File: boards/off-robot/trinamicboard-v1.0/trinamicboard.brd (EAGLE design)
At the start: 133.7 x 89.7 mm, 57 parts, among them J4 DF22-2, J5 4-PIN_2MM-H, J6 MKS-1658, U1 ADC124S101, U2 SN74LVC3G17, U3 SN74LVC3G17, U4 VND5E006ASPTR-E, U5 MPM3620GQV-P, U6 MPM3620GQV-P

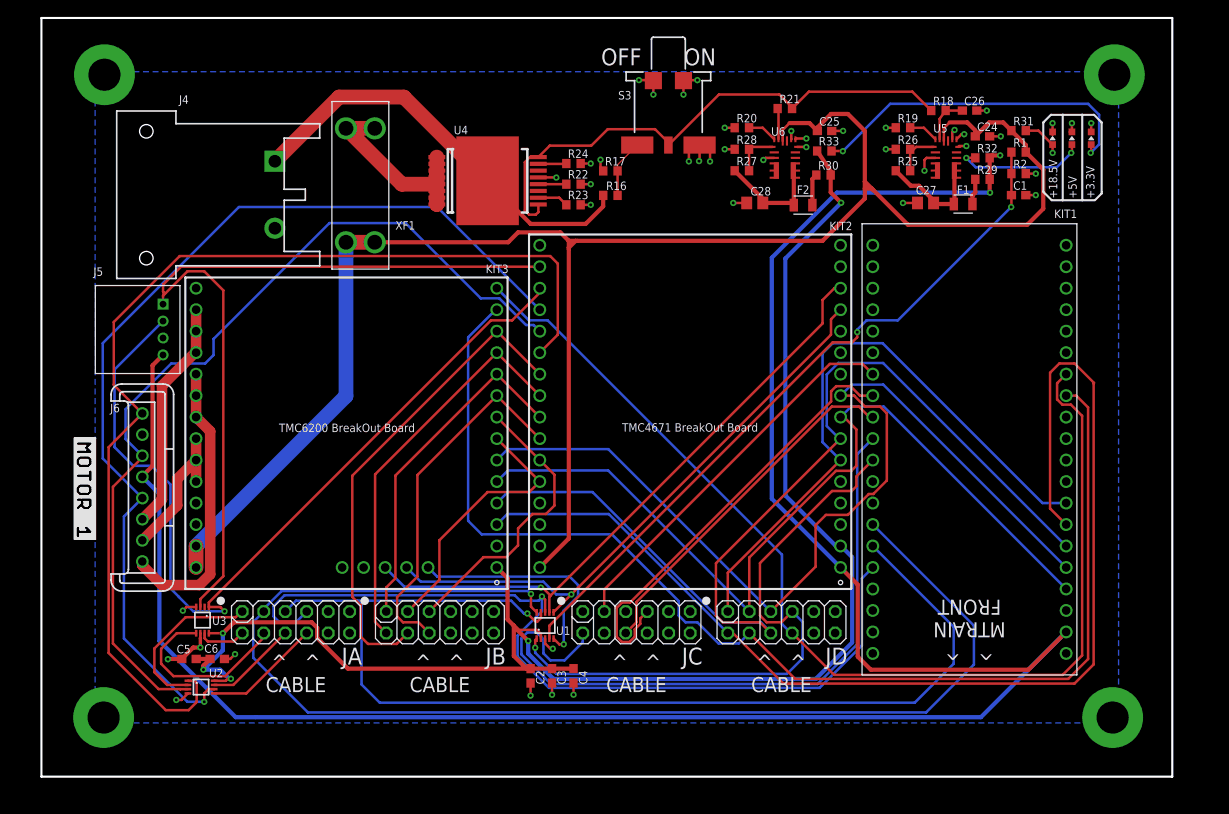
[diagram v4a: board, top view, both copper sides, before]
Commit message: Renumbered silkscreen Added "Summer 2020" to bPlace
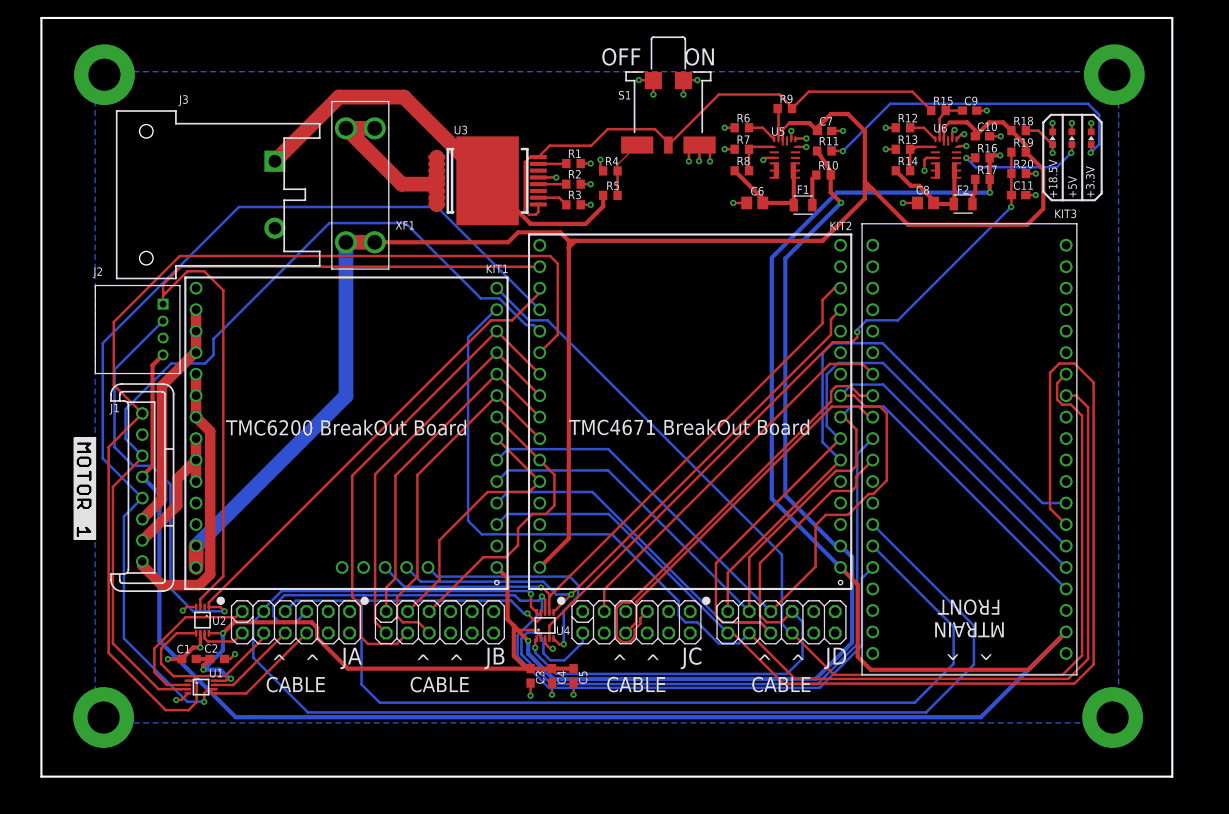
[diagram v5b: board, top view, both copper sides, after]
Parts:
- removed C28: 22uF 16V, rcl:C0805
- removed D4: GREEN, RoboJackets-LEDs:CHIP-LED0603
- removed R22: 10k, rcl:R0603
- removed R24, R31: 1k, rcl:R0603
- removed R29: 0, resistor:R0603
- removed R32: 1k, resistor:R0603
- added C11: 0.1uF 50V, resistor:C0603
- added D1: GREEN, RoboJackets-LEDs:CHIP-LED0603
- added R12: 43.2k, rcl:R0603
- added R15: 150k, rcl:R0603
- added R4: 100k, rcl:R0603
- added R5: 270k, rcl:R0603
- added R6: 29.4k, rcl:R0603
- C1: value 0.1uF 50V -> 0.1uF
- C2: value 0.01uF -> 0.1uF
- C3: value 0.1uF -> 0.01uF
- C4: value 1uF -> 0.1uF
- C5: value 0.1uF -> 1uF
- C6: value 0.1uF -> 22uF 16V; device resistor:C0603 -> rcl:C0805
- KIT1: value MTRAIN -> (none); device RoboJackets-Boards:MTRAIN-KIT -> RoboJackets-Boards:TMC6200-BOB
- KIT3: value (none) -> MTRAIN; device RoboJackets-Boards:TMC6200-BOB -> RoboJackets-Boards:MTRAIN-KIT
- R1: value 68k 1% -> 1k; device resistor:R0603 -> rcl:R0603
- R16: value 270k -> 1k; device rcl:R0603 -> resistor:R0603
- R17: value 100k -> 0; device rcl:R0603 -> resistor:R0603
- R18: value 150k -> 1k
- R19: value 43.2k -> 68k 1%; device rcl:R0603 -> resistor:R0603
- R2: value 10k 1% -> 10k; device resistor:R0603 -> rcl:R0603
- R20: value 29.4k -> 10k 1%; device rcl:R0603 -> resistor:R0603
- U1: value ADC124S101 -> SN74LVC3G17; device RoboJackets-ICs:VSSOP-10 -> RoboJackets-ICs:VSSOP-8
- U3: value SN74LVC3G17 -> VND5E006ASPTR-E; device RoboJackets-ICs:VSSOP-8 -> RoboJackets-PowerICs:POWERSO-16
- U4: value VND5E006ASPTR-E -> ADC124S101; device RoboJackets-PowerICs:POWERSO-16 -> RoboJackets-ICs:VSSOP-10
- moved C1 112.4 mm to (-52.9, -18.4), turned to 180 degrees
- moved C6 83.3 mm to (14.0, 35.5), turned to 180 degrees
- moved KIT1 73.7 mm to (-34.3, 8.89)
- moved KIT3 73.7 mm to (39.4, 6.35)
- moved U3 61.9 mm to (-17.6, 38.1)
- moved U4 53.0 mm to (-11.0, -14.5), turned to 90 degrees
- moved R1 52.6 mm to (-7.45, 40.1)
- moved R2 52.6 mm to (-7.45, 37.7), turned to 180 degrees
- moved C5 45.5 mm to (-7.44, -20.4), turned to 270 degrees
- moved R16 44.2 mm to (40.9, 40.8)
- moved R17 44.0 mm to (40.9, 38.3)
- moved U1 41.1 mm to (-51.5, -21.8), turned to 0 degrees
- moved C2 37.1 mm to (-49.6, -18.4), turned to 0 degrees
- moved R20 33.2 mm to (45.2, 38.9)
- moved U5 19.0 mm to (17.5, 40.6)
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- renumbered C24 to C10, C25 to C7, C26 to C9, C27 to C8, J4 to J3, J5 to J2, J6 to J1, R21 to R9, R23 to R3, R25 to R14, R26 to R13, R27 to R8, R28 to R7, R30 to R10, R33 to R11, S3 to S1, U$11 to U$101, U$2 to U$100, U$3 to U$1
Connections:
- net !SS!-4671: now also KIT3.P$8; no longer KIT1.P$8
- net !SS!-6200: now also KIT1.3, KIT3.P$7; no longer KIT1.P$7, KIT3.3
- net !SS!-ADC: now also KIT3.P$31, U4.1; no longer KIT1.P$31, U1.1
- net !SS!-FPGA: now also KIT3.P$30; no longer KIT1.P$30
- net +18.5V: now also KIT1.15, KIT1.16, R18.2, R19.1; no longer KIT3.15, KIT3.16, R1.1, R31.2
- net +3.3V: now also C1.1, KIT1.1, U1.8, U4.2; no longer C6.1, KIT3.1, U1.2, U3.8
- net +3.3V-FUSE: now also C6.1, F1.1, U5.789; no longer C28.1, F2.1, U6.789
- net +3.3V-LED: now also D3.A; no longer D4.A
- net +3.3V-PREFUSE: now also F1.2; no longer F2.2
- net +5V: now also KIT3.VIN, R16.1, R17.2; no longer KIT1.VIN, R29.2, R32.1
- net +5V-FUSE: now also F2.1, U6.789; no longer F1.1, U5.789
- net +5V-LED: now also D2.A, R16.2; no longer D3.A, R32.2
- net +5V-PREFUSE: now also F2.2, R17.1; no longer F1.2, R29.1
- net 18.5V-LED: now also D1.A, R18.1; no longer D2.A, R31.1
- net AAM: now also R12.2, U6.18; no longer R19.2, U5.18
- net AAM1: now also R6.2, U5.18; no longer R20.2, U6.18
- net CS-DIS: now also R2.2, U3.12; no longer R22.2, U4.12
- net CS1: now also U3.10; no longer U4.10
- net CS2: now also R1.2, U3.15; no longer R24.2, U4.15
- net CURU: now also KIT1.31, U4.7; no longer KIT3.31, U1.7
- net CURV: now also KIT1.30, U4.6; no longer KIT3.30, U1.6
- net CURW: now also KIT1.29, U4.5; no longer KIT3.29, U1.5
- net DRV_EN: now also KIT1.13, KIT3.P$13; no longer KIT1.P$13, KIT3.13
- net EN: now also R15.2, U6.17; no longer R18.2, U5.17
- net EN-PWR: now also R15.1, U3.16, U3.9; no longer R18.1, U4.16, U4.9
- net EN-PWR-PRE: now also R4.2, R5.1; no longer R16.1, R17.2
- net EN1: now also U5.17; no longer U6.17
- net ENC-A: now also U2.1; no longer U3.1
- net ENC-B: now also U2.3; no longer U3.3
- net ENC1-A: now also U2.7; no longer U3.7
- net ENC1-B: now also U2.5; no longer U3.5
- net FAULT: now also KIT1.14, KIT3.P$14; no longer KIT1.P$14, KIT3.14
- net FB: now also U6.1; no longer U5.1
- net FB1: now also U5.1; no longer U6.1
- net GND: now also C11.2, D1.C, KIT1.17, KIT1.18, KIT1.2, KIT1.28, KIT1.32, KIT3.GND, R1.1, R12.1, R2.1, R20.2, R4.1, R6.1, U1.4, U2.6, U3.13, U4.3; no longer C28.2, D4.C, KIT1.GND, KIT3.17, KIT3.18, KIT3.2, KIT3.28, KIT3.32, R17.1, R19.1, R2.2, R20.1, R22.1, R24.1, U1.3, U3.4, U3.6, U4.13
- net H1: now also U1.1; no longer U2.1
- net H2: now also U1.3; no longer U2.3
- net H3: now also U1.6; no longer U2.6
- net HALL-U: now also U1.7; no longer U2.7
- net HALL-V: now also U1.5; no longer U2.5
- net HALL-W: now also U1.2; no longer U2.2
- net MISO-ADC: now also KIT3.P$35, U4.9; no longer KIT1.P$35, U1.9
- net MISO-FPGA: now also KIT3.P$28; no longer KIT1.P$28
- net MISO-TMC: now also KIT1.6, KIT3.P$5; no longer KIT1.P$5, KIT3.6
- net MOSI-ADC: now also KIT3.P$36, U4.8; no longer KIT1.P$36, U1.8
- net MOSI-FPGA: now also KIT3.P$27; no longer KIT1.P$27
- net MOSI-TMC: now also KIT1.5, KIT3.P$4; no longer KIT1.P$4, KIT3.5
- net PHASE-A: now also KIT1.19, KIT1.20, KIT1.21; no longer KIT3.19, KIT3.20, KIT3.21
- net PHASE-B: now also KIT1.22, KIT1.23, KIT1.24; no longer KIT3.22, KIT3.23, KIT3.24
- net PHASE-C: now also KIT1.25, KIT1.26, KIT1.27; no longer KIT3.25, KIT3.26, KIT3.27
- net PWM-UH: now also KIT1.12; no longer KIT3.12
- net PWM-UL: now also KIT1.11; no longer KIT3.11
- net PWM-VH: now also KIT1.10; no longer KIT3.10
- net PWM-VL: now also KIT1.9; no longer KIT3.9
- net PWM-WH: now also KIT1.8; no longer KIT3.8
- net PWM-WL: now also KIT1.7; no longer KIT3.7
- net SCK-ADC: now also KIT3.P$34, U4.10; no longer KIT1.P$34, U1.10
- net SCK-FPGA: now also KIT3.P$29; no longer KIT1.P$29
- net SCK-TMC: now also KIT1.4, KIT3.P$6; no longer KIT1.P$6, KIT3.4
- net SENSE-SUPPLY: now also C11.1, R19.2, R20.1, U4.4; no longer C1.1, R1.2, R2.1, U1.4
- net SW: now also U6.456; no longer U5.456
- net SW1: now also U5.456; no longer U6.456
- net VBATT: now also U3.1, U3.2, U3.3, U3.4, U3.5, U3.6, U3.7, U3.8; no longer U4.1, U4.2, U4.3, U4.4, U4.5, U4.6, U4.7, U4.8
- net VBUS: now also KIT3.VBUS; no longer KIT1.VBUS
- net VDD: now also KIT3.VDD; no longer KIT1.VDD
- net VIN: now also R5.2, U3.17; no longer R16.2, U4.17
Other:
- board text added: "Summer 2020"

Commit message: Changed Robojackets bottom img
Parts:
- removed U$101: (no value), RoboJackets-Aesthetics:ROBOBUZZ_1.0X2
- added U$2: (no value), RoboJackets-Aesthetics:ROBOBUZZ_1.4X
- moved U$100 6.58 mm to (19.6, 16.7)
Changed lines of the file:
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@@
 <layer number="19" name="Unrouted" color="6" fill="1" visible="yes" active="yes"/>
 <layer number="20" name="Dimension" color="24" fill="1" visible="yes" active="yes"/>
-<layer number="21" name="tPlace" color="7" fill="1" visible="yes" active="yes"/>
+<layer number="21" name="tPlace" color="7" fill="1" visible="no" active="yes"/>
 <layer number="22" name="bPlace" color="7" fill="1" visible="yes" active="yes"/>
 <layer number="23" name="tOrigins" color="15" fill="1" visible="no" active="yes"/>
@@
 <text x="0.6" y="53.75" size="2" layer="21" font="vector" ratio="15" rot="R180">OFF</text>
 <text x="9.4" y="53.75" size="2" layer="21" font="vector" ratio="15" rot="R180">ON</text>
-<text x="20.5" y="18" size="2" layer="22" font="vector" ratio="15" rot="MR0">Trinamic</text>
-<text x="8.9" y="18" size="2" layer="22" ratio="15" rot="MR0">v1.0</text>
+<text x="7.5" y="8.7" size="2" layer="22" font="vector" ratio="15" rot="MR0">Trinamic</text>
+<text x="-3.9" y="8.7" size="2" layer="22" ratio="15" rot="MR0">v1.0</text>
 <polygon width="0.1524" layer="22">
 <vertex x="20" y="4"/>
@@
 <wire x1="55" y1="36.6" x2="54.2" y2="35.8" width="0.25" layer="21"/>
 <wire x1="55" y1="36.8" x2="55" y2="36.6" width="0.25" layer="21"/>
-<text x="20.5" y="14.9" size="1.5" layer="22" font="vector" rot="MR0">Summer 2020</text>
+<text x="7.5" y="5.9" size="1.5" layer="22" font="vector" rot="MR0">Summer 2020</text>
 </plain>
 <attributes>
@@
 </element>
 <element name="U$1" library="RoboJackets-Aesthetics" package="MOTOR-1" value="" x="-66.45" y="7.71" smashed="yes" rot="R270"/>
-<element name="U$101" library="RoboJackets-Aesthetics" package="ROBOBUZZ_1.0X2" value="" x="-1.6" y="3.4" smashed="yes" rot="SMR0"/>
-<element name="U$100" library="RoboJackets-Aesthetics" package="ROBOJACKETS" value="" x="20.6" y="23.16" smashed="yes" rot="MR0"/>
+<element name="U$100" library="RoboJackets-Aesthetics" package="ROBOJACKETS" value="" x="19.6" y="16.66" smashed="yes" rot="MR0"/>
+<element name="U$2" library="RoboJackets-Aesthetics" package="ROBOBUZZ_1.4X" value="" x="-34" y="-3" smashed="yes" rot="MR0"/>
 </elements>
 <signals>

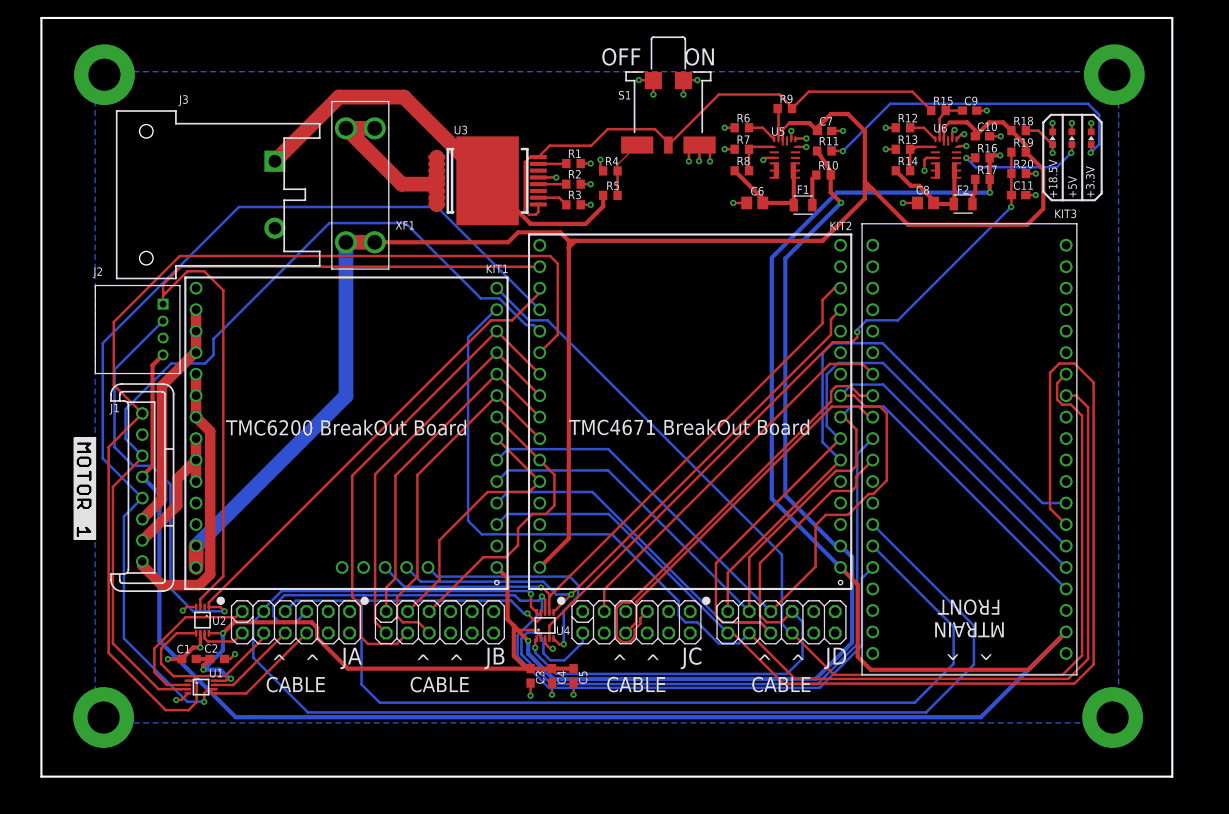
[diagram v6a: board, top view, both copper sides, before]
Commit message: Passed ERC, DRC, adjusted silkscreen and routing slightly
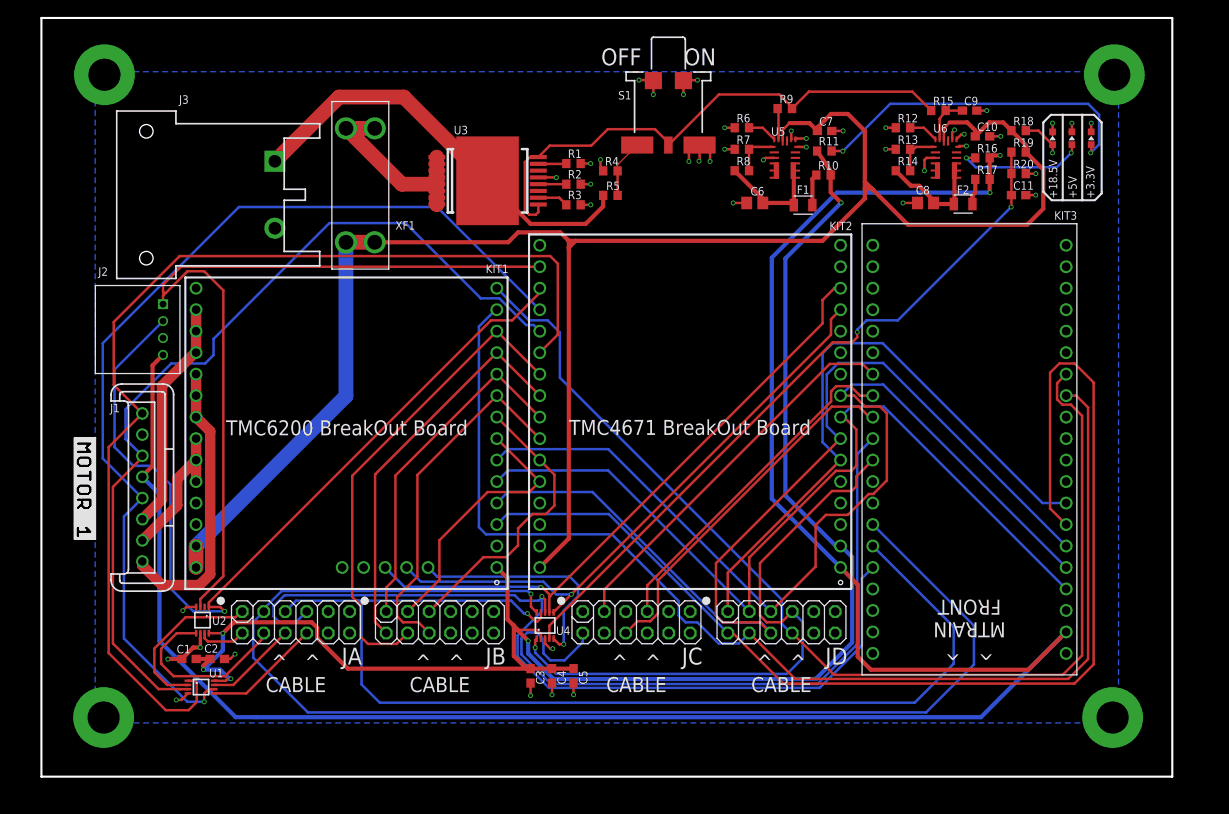
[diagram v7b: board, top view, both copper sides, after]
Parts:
- moved U$100 0.62 mm to (19.0, 16.5)
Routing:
- net MISO-FPGA: track 52.0 -> 40.7 mm
- net DRV_EN: track 143.4 -> 142.0 mm
- net SCK-FPGA: track 42.2 -> 43.1 mm
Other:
- board text added: ">VERSION"
- board text removed: "v1.0"
